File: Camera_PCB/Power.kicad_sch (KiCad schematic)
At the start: 50 parts, among them J3 USB_C_Receptacle_PowerOnly_6P, Q3 AO3400A, Q4 AO3400A, SW2 SW_Push, U4 BQ297xy

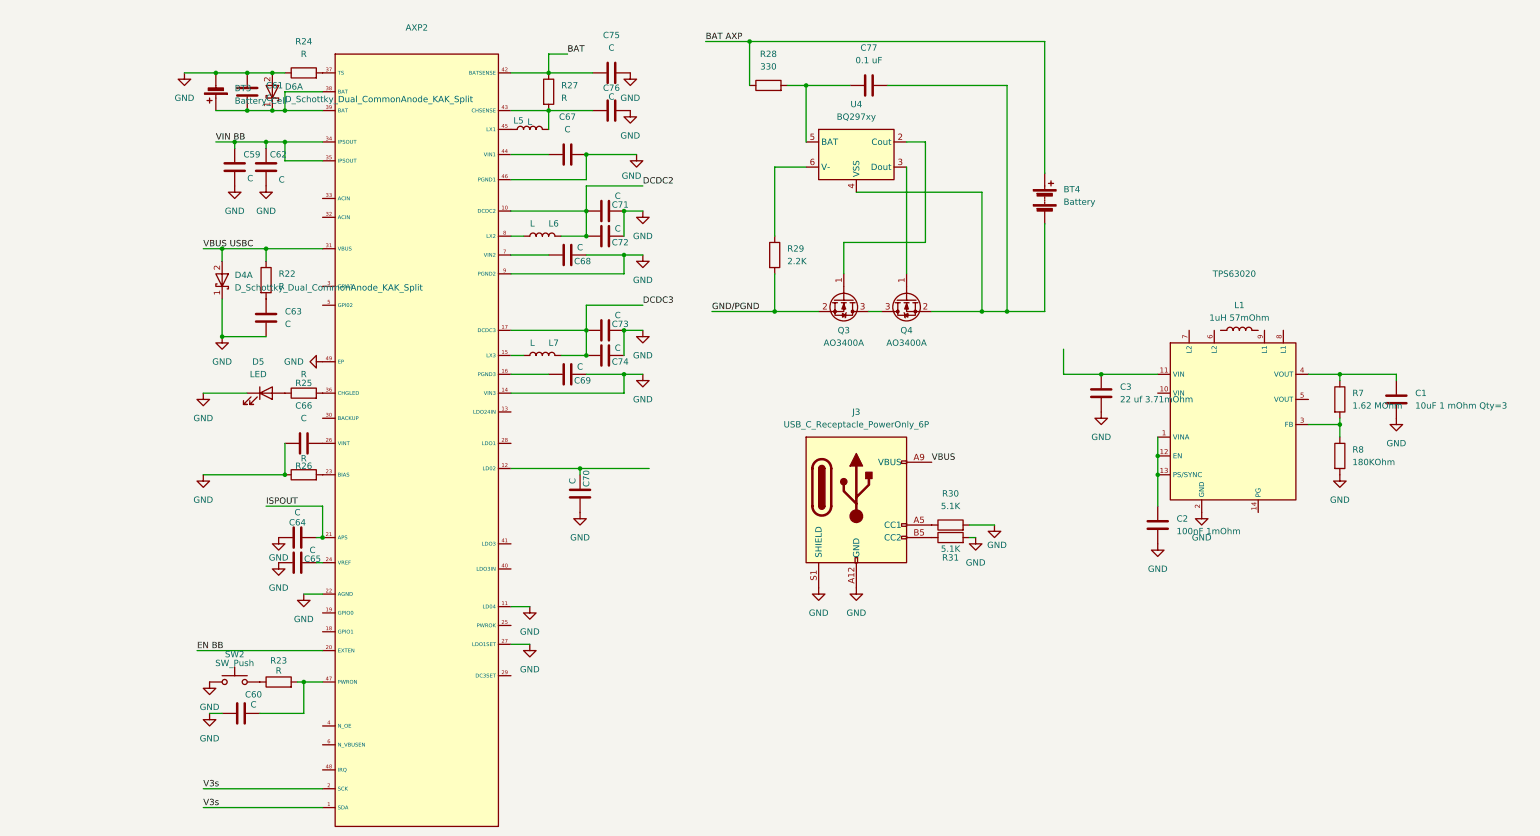
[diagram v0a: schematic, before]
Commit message: Updated Component Values for Power
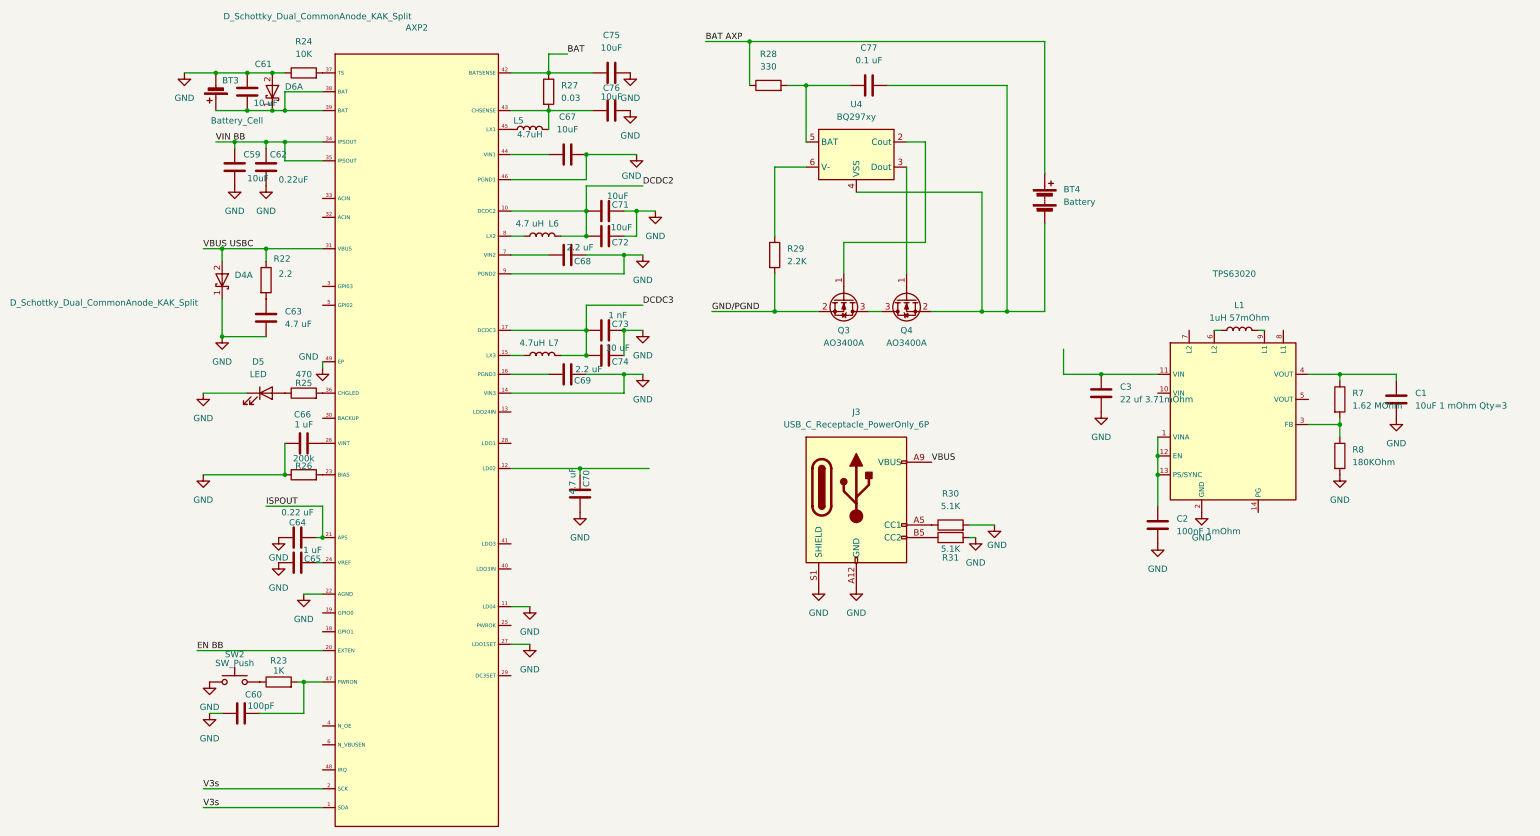
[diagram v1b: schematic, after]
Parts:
- C59, C67, C71, C72, C75, C76: value C -> 10uF
- C60: value C -> 100pF
- C61, C74: value C -> 10 uF
- C62: value C -> 0.22uF
- C63, C70: value C -> 4.7 uF
- C64: value C -> 0.22 uF
- C65, C66: value C -> 1 uF
- C68, C69: value C -> 2.2 uF
- C73: value C -> 1 nF
- L5, L7: value L -> 4.7uH
- L6: value L -> 4.7 uH
- R22: value R -> 2.2
- R23: value R -> 1K
- R24: value R -> 10K
- R25: value R -> 470
- R26: value R -> 200k
- R27: value R -> 0.03
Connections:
- net at TPS63020.6 (L2): now also L1.1
- net at TPS63020.9 (L1): now also L1.2
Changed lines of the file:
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@@
 	)
 	(junction
-		(at 114.3 60.96)
-		(diameter 0)
-		(color 0 0 0 0)
-	)
-	(junction
 		(at 43.18 40.64)
 		(diameter 0)
@@
 	)
 	(junction
+		(at 116.84 60.96)
+		(diameter 0)
+		(color 0 0 0 0)
+	)
+	(junction
 		(at 106.68 90.17)
 		(diameter 0)
@@
 	(wire
 		(pts
+			(xy 233.68 85.09) (xy 234.95 85.09)
+		)
+		(stroke
+			(width 0)
+			(type default)
+		)
+	)
+	(wire
+		(pts
 			(xy 222.25 114.3) (xy 222.25 120.65)
 		)
@@
 	(wire
 		(pts
+			(xy 53.34 92.71) (xy 53.34 91.44)
+		)
+		(stroke
+			(width 0)
+			(type default)
+		)
+	)
+	(wire
+		(pts
 			(xy 29.21 97.79) (xy 38.1 97.79)
 		)
@@
 	(wire
 		(pts
+			(xy 116.84 60.96) (xy 120.65 60.96)
+		)
+		(stroke
+			(width 0)
+			(type default)
+		)
+	)
+	(wire
+		(pts
 			(xy 199.39 26.67) (xy 139.7 26.67)
 		)
@@
 	(wire
 		(pts
-			(xy 114.3 60.96) (xy 114.3 66.04)
+			(xy 116.84 60.96) (xy 116.84 66.04)
 		)
 		(stroke
@@
 	(wire
 		(pts
+			(xy 242.57 85.09) (xy 243.84 85.09)
+		)
+		(stroke
+			(width 0)
+			(type default)
+		)
+	)
+	(wire
+		(pts
 			(xy 259.08 93.98) (xy 259.08 95.25)
 		)
@@
 	(wire
 		(pts
-			(xy 114.3 60.96) (xy 118.11 60.96)
+			(xy 114.3 60.96) (xy 116.84 60.96)
 		)
 		(stroke
@@
 	(wire
 		(pts
+			(xy 116.84 66.04) (xy 114.3 66.04)
+		)
+		(stroke
+			(width 0)
+			(type default)
+		)
+	)
+	(wire
+		(pts
 			(xy 99.06 40.64) (xy 99.06 44.45)
 		)
@@
 			)
 		)
-		(property "Value" "C"
+		(property "Value" "2.2 uF"
 			(at 105.41 68.326 90)
 			(effects
@@
 			)
 		)
-		(property "Value" "C"
-			(at 39.37 160.782 90)
+		(property "Value" "100pF"
+			(at 40.894 161.036 90)
 			(effects
 				(font
@@
 			)
 		)
-		(property "Value" "R"
+		(property "Value" "470"
 			(at 49.53 93.98 90)
 			(effects
@@
 			)
 		)
-		(property "Value" "C"
+		(property "Value" "10uF"
 			(at 111.76 37.846 90)
 			(effects
@@
 			)
 		)
-		(property "Value" "C"
+		(property "Value" "0.22uF"
 			(at 44.45 54.61 0)
 			(effects
@@
 		(on_board yes)
 		(dnp no)
-		(fields_autoplaced yes)
 		(property "Reference" "BT3"
-			(at 35.56 36.1314 0)
+			(at 33.02 34.544 0)
 			(effects
 				(font
@@
 		)
 		(property "Value" "Battery_Cell"
-			(at 35.56 38.6714 0)
+			(at 30.734 42.672 0)
 			(effects
 				(font
@@
 			)
 		)
-		(property "Value" "C"
+		(property "Value" "4.7 uF"
 			(at 103.886 115.57 90)
 			(effects
@@
 			)
 		)
-		(property "Value" "C"
-			(at 105.41 92.456 90)
+		(property "Value" "2.2 uF"
+			(at 107.188 92.964 90)
 			(effects
 				(font
@@
 			)
 		)
-		(property "Value" "C"
+		(property "Value" "4.7 uF"
 			(at 45.72 83.8199 0)
 			(effects
@@
 			)
 		)
-		(property "Value" "C"
+		(property "Value" "1 uF"
 			(at 51.308 129.54 90)
 			(effects
@@
 			)
 		)
-		(property "Value" "R"
+		(property "Value" "200k"
 			(at 49.53 110.998 90)
 			(effects
@@
 	(symbol
 		(lib_id "power:GND")
-		(at 53.34 91.44 270)
+		(at 53.34 92.71 0)
 		(unit 1)
 		(exclude_from_sim no)
@@
 		(on_board yes)
 		(dnp no)
-		(fields_autoplaced yes)
 		(property "Reference" "#PWR038"
-			(at 46.99 91.44 0)
+			(at 53.34 99.06 0)
 			(effects
 				(font
@@
 		)
 		(property "Value" "GND"
-			(at 49.53 91.4399 90)
+			(at 48.514 90.424 0)
 			(effects
 				(font
 					(size 1.27 1.27)
 				)
-				(justify right)
+				(justify left)
 			)
 		)
 		(property "Footprint" ""
-			(at 53.34 91.44 0)
+			(at 53.34 92.71 0)
 			(effects
 				(font
@@
 		)
 		(property "Datasheet" ""
-			(at 53.34 91.44 0)
+			(at 53.34 92.71 0)
 			(effects
 				(font
@@
 		)
 		(property "Description" "Power symbol creates a global label with name \"GND\" , ground"
-			(at 53.34 91.44 0)
+			(at 53.34 92.71 0)
 			(effects
 				(font
@@
 			)
 		)
-		(property "Value" "L"
-			(at 95.25 42.926 90)
+		(property "Value" "4.7uH"
+			(at 95.25 45.466 90)
 			(effects
 				(font
@@
 			)
 		)
-		(property "Value" "C"
+		(property "Value" "10 uF"
 			(at 113.03 88.646 90)
 			(effects
@@
 			)
 		)
-		(property "Value" "C"
+		(property "Value" "10uF"
 			(at 113.03 57.912 90)
 			(effects
@@
 			)
 		)
-		(property "Value" "R"
+		(property "Value" "0.03"
 			(at 101.6 38.0999 0)
 			(effects
@@
 	(symbol
 		(lib_id "power:GND")
-		(at 118.11 60.96 0)
+		(at 120.65 60.96 0)
 		(unit 1)
 		(exclude_from_sim no)
@@
 		(fields_autoplaced yes)
 		(property "Reference" "#PWR046"
-			(at 118.11 67.31 0)
+			(at 120.65 67.31 0)
 			(effects
 				(font
@@
 		)
 		(property "Value" "GND"
-			(at 118.11 66.04 0)
+			(at 120.65 66.04 0)
 			(effects
 				(font
@@
 		)
 		(property "Footprint" ""
-			(at 118.11 60.96 0)
+			(at 120.65 60.96 0)
 			(effects
 				(font
@@
 		)
 		(property "Datasheet" ""
-			(at 118.11 60.96 0)
+			(at 120.65 60.96 0)
 			(effects
 				(font
@@
 		)
 		(property "Description" "Power symbol creates a global label with name \"GND\" , ground"
-			(at 118.11 60.96 0)
+			(at 120.65 60.96 0)
 			(effects
 				(font
@@
 			)
 		)
-		(property "Value" "C"
+		(property "Value" "0.22 uF"
 			(at 48.26 121.92 90)
 			(effects
@@
 			)
 		)
-		(property "Value" "R"
+		(property "Value" "1K"
 			(at 44.45 153.924 90)
 			(effects
@@
 			)
 		)
-		(property "Value" "R"
+		(property "Value" "10K"
 			(at 49.53 29.21 90)
 			(effects
@@
 			)
 		)
-		(property "Value" "C"
+		(property "Value" "1 nF"
 			(at 113.03 82.042 90)
 			(effects
@@
 			)
 		)
-		(property "Value" "C"
+		(property "Value" "10uF"
 			(at 111.76 27.94 90)
 			(effects
@@
 			)
 		)
-		(property "Value" "C"
+		(property "Value" "10uF"
 			(at 38.1 54.356 0)
 			(effects
@@
 		(on_board yes)
 		(dnp no)
-		(fields_autoplaced yes)
 		(property "Reference" "R22"
-			(at 44.45 73.6599 0)
+			(at 43.434 70.612 0)
 			(effects
 				(font
@@
 			)
 		)
-		(property "Value" "R"
-			(at 44.45 76.1999 0)
+		(property "Value" "2.2"
+			(at 44.45 73.66 0)
 			(effects
 				(font
@@
 			)
 		)
-		(property "Value" "C"
-			(at 113.03 64.516 90)
+		(property "Value" "10uF"
+			(at 113.792 64.262 90)
 			(effects
 				(font
@@
 		(on_board yes)
 		(dnp no)
-		(fields_autoplaced yes)
 		(property "Reference" "C66"
-			(at 49.53 100.33 90)
+			(at 49.276 102.108 90)
 			(effects
 				(font
@@
 			)
 		)
-		(property "Value" "C"
-			(at 49.53 102.87 90)
+		(property "Value" "1 uF"
+			(at 49.53 104.14 90)
 			(effects
 				(font
@@
 		)
 		(property "Value" "D_Schottky_Dual_CommonAnode_KAK_Split"
-			(at 35.56 76.4539 90)
+			(at -9.906 79.502 90)
 			(effects
 				(font
@@
 			)
 		)
-		(property "Value" "L"
+		(property "Value" "4.7uH"
 			(at 95.758 87.63 90)
 			(effects
@@
 			)
 		)
-		(property "Value" "C"
+		(property "Value" "10uF"
 			(at 102.87 44.45 90)
 			(effects
@@
 		)
 		(property "Value" "D_Schottky_Dual_CommonAnode_KAK_Split"
-			(at 45.72 38.3539 90)
+			(at 33.274 21.59 90)
 			(effects
 				(font
@@
 		(on_board yes)
 		(dnp no)
-		(fields_autoplaced yes)
 		(property "Reference" "C61"
-			(at 41.91 35.5599 0)
+			(at 39.624 31.242 0)
 			(effects
 				(font
@@
 			)
 		)
-		(property "Value" "C"
-			(at 41.91 38.0999 0)
+		(property "Value" "10 uF"
+			(at 39.37 39.116 0)
 			(effects
 				(font
@@
 			)
 		)
-		(property "Value" "L"
-			(at 95.758 63.5 90)
+		(property "Value" "4.7 uH"
+			(at 95.25 63.5 90)
 			(effects
 				(font

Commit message: 10/29 Footprint Additions
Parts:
- AXP2: Distributor (none) -> Aliexpress
- C1: value 10uF 1 mOhm Qty=3 -> 10u; footprint (none) -> Capacitor_SMD:C_0805_2012Metric_Pad1.18x1.45mm_HandSolder
- C2: value 100nF 1mOhm -> 100n; footprint (none) -> Capacitor_SMD:C_0603_1608Metric_Pad1.08x0.95mm_HandSolder
- C3: value 22 uf 3.71mOhm -> 22u; footprint (none) -> Capacitor_SMD:C_0805_2012Metric_Pad1.18x1.45mm_HandSolder
- C59, C67, C71, C72, C75, C76: value 10uF -> 10u; footprint (none) -> Capacitor_SMD:C_0805_2012Metric_Pad1.18x1.45mm_HandSolder
- C60: value 100pF -> 100p; footprint (none) -> Capacitor_SMD:C_0603_1608Metric_Pad1.08x0.95mm_HandSolder
- C61, C74: value 10 uF -> 10u; footprint (none) -> Capacitor_SMD:C_0805_2012Metric_Pad1.18x1.45mm_HandSolder
- C62: value 0.22uF -> 0.22u; footprint (none) -> Capacitor_SMD:C_0603_1608Metric_Pad1.08x0.95mm_HandSolder
- C63, C70: value 4.7 uF -> 4.7u; footprint (none) -> Capacitor_SMD:C_0805_2012Metric_Pad1.18x1.45mm_HandSolder
- C64: value 0.22 uF -> 0.22u; footprint (none) -> Capacitor_SMD:C_0603_1608Metric_Pad1.08x0.95mm_HandSolder
- C65, C66: value 1 uF -> 1u; footprint (none) -> Capacitor_SMD:C_0805_2012Metric_Pad1.18x1.45mm_HandSolder
- C68, C69: value 2.2 uF -> 2.2u; footprint (none) -> Capacitor_SMD:C_0805_2012Metric_Pad1.18x1.45mm_HandSolder
- C73: value 1 nF -> 1n; footprint (none) -> Capacitor_SMD:C_0603_1608Metric_Pad1.08x0.95mm_HandSolder
- C77: value 0.1 uF -> 0.1u; footprint (none) -> Capacitor_SMD:C_0603_1608Metric_Pad1.08x0.95mm_HandSolder
- J3: footprint (none) -> Connector_USB:USB_C_Receptacle_GCT_USB4085; DPN (none) -> USB4085-GF-A; Distributor (none) -> DigiKey
- TPS63020: DPN (none) -> TPS63020DSJT; Distributor (none) -> Digikey
- U4: DPN (none) -> BQ29700DSET; Distributor (none) -> Digikey

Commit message: Camera PCB Schematic review 1
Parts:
- removed BT3: Battery_Cell, symbol Device:Battery_Cell
- removed BT4: Battery, symbol Device:Battery
- removed C1, C59, C61, C67, C71, C72, C74, C75, C76: 10u, Capacitor_SMD:C_0805_2012Metric_Pad1.18x1.45mm_HandSolder, symbol Device:C
- removed C2: 100n, Capacitor_SMD:C_0603_1608Metric_Pad1.08x0.95mm_HandSolder, symbol Device:C
- removed C3: 22u, Capacitor_SMD:C_0805_2012Metric_Pad1.18x1.45mm_HandSolder, symbol Device:C
- removed C60: 100p, Capacitor_SMD:C_0603_1608Metric_Pad1.08x0.95mm_HandSolder, symbol Device:C
- removed C62, C64: 0.22u, Capacitor_SMD:C_0603_1608Metric_Pad1.08x0.95mm_HandSolder, symbol Device:C
- removed C63, C70: 4.7u, Capacitor_SMD:C_0805_2012Metric_Pad1.18x1.45mm_HandSolder, symbol Device:C
- removed C65, C66: 1u, Capacitor_SMD:C_0805_2012Metric_Pad1.18x1.45mm_HandSolder, symbol Device:C
- removed C68, C69: 2.2u, Capacitor_SMD:C_0805_2012Metric_Pad1.18x1.45mm_HandSolder, symbol Device:C
- removed C73: 1n, Capacitor_SMD:C_0603_1608Metric_Pad1.08x0.95mm_HandSolder, symbol Device:C
- removed C77: 0.1u, Capacitor_SMD:C_0603_1608Metric_Pad1.08x0.95mm_HandSolder, symbol Device:C
- removed D4, D6: D_Schottky_Dual_CommonAnode_KAK_Split, symbol Device:D_Schottky_Dual_CommonAnode_KAK_Split
- removed D5: LED, symbol Device:LED
- removed L1: 1uH 57mOhm, symbol Device:L
- removed L6: 4.7 uH, symbol Device:L
- removed L7: 4.7uH, symbol Device:L
- removed Q3, Q4: AO3400A, Package_TO_SOT_SMD:SOT-23, symbol Transistor_FET:AO3400A
- removed R22: 2.2, symbol Device:R
- removed R23: 1K, symbol Device:R
- removed R24: 10K, symbol Device:R
- removed R25: 470, symbol Device:R
- removed R26: 200k, symbol Device:R
- removed R27: 0.03, symbol Device:R
- removed R28: 330, symbol Device:R
- removed R29: 2.2K, symbol Device:R
- removed R30, R31: 5.1K, symbol Device:R
- removed R7: 1.62 MOhm, symbol Device:R
- removed R8: 180KOhm, symbol Device:R
- removed SW2: SW_Push, symbol Switch:SW_Push
- removed TPS63020: ~, BackupCamCustomParts:IC_TPS63020DSJT, symbol Senior:TPS63020
- removed U4: BQ297xy, Package_SON:WSON-6_1.5x1.5mm_P0.5mm, symbol Battery_Management:BQ297xy
- added BT1: Battery_Cell, symbol Device:Battery_Cell
- added C35, C42, C43, C50, C54, C56, C58, C6, C62, C63: 10u, symbol Device:C_Small
- added C36, C44, C61, C73, C74: 4.7u, symbol Device:C_Small
- added C45, C55, C57, C59, C60: 0.1u, symbol Device:C_Small
- added C48, C49, C5: 1u, symbol Device:C_Small
- added L8, L9: 4.7uH, symbol Device:L
- added R14: 0.03, symbol Device:R_Small_US
- added R15: 200k, symbol Device:R_Small_US
- added R16, R17: 5.1k, symbol Device:R_Small_US
- added R20, R21: 1k, symbol Device:R_Small_US
- added R22, R23: 0, symbol Device:R_Small_US
- added SW1: PWR, symbol Switch:SW_MEC_5E
- added SW2: RST, symbol Switch:SW_MEC_5E
- U1: renamed from AXP2; value ~ -> AXP203; symbol Senior:AXP203 -> custom_chips:AXP203; Distributor Aliexpress -> (none)
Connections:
- net BAT is gone; now on net VBAT: U1.42 (BATSENSE)
- net ISPOUT is gone; now on net VIPS: U1.21 (APS)
- net VIN BB is gone; now on net VIPS: U1.34 (IPSOUT), U1.35 (IPSOUT)
- net GND: now also U1.16 (PGND3), U1.29 (DC3SET), BT1.2 (-), C35.2, C36.2, C42.1, C43.1, C50.1, C54.1, C55.1, C56.1, C57.1, C58.1, C6.2, C61.1, C62.1, C63.1, C73.1, C74.1, R16.2, R17.2; no longer U1.11 (LD04), U1.14 (VIN3), U1.22 (AGND), U1.27 (LDO1SET)
- net VBUS: now also U1.32 (ACIN), U1.33 (ACIN), C50.2
- net at J3.A5 (CC1): now also R17.1
- net at J3.B5 (CC2): now also R16.1
- net VIPS: now reaches U1.7 (VIN2)
- net VIPS: now also U1.14 (VIN3), U1.44 (VIN1), C36.1, C42.2, C43.2, C44.1, C45.1, C58.2, R22.1
- net at U1.47 (PWRON): now also C59.1, R20.2
- net CHGLED: now reaches U1.36 (CHGLED)
- net at L5.2, U1.43 (CHSENSE): now also C5.2, C6.1, R14.1
- net VBAT: now reaches U1.38 (BAT), U1.39 (BAT)
- net VBAT: now also BT1.1 (+), C35.1, C5.1, R14.2
- net +3V0: now reaches U1.12 (LD02)
- net +3V0: now also C63.2
- net at U1.24 (VREF): now also C48.1
- net at U1.23 (BIAS): now also R15.2
- net +3V3: now reaches U1.13 (LDO24IN)
- net +3V3: now also C62.2
- net at U1.15 (LX3): now also L9.1
- net PGOOD: now reaches U1.25 (PWROK)
- net VINT: now reaches U1.26 (VINT)
- net VINT: now also U1.27 (LDO1SET), C49.2
- net VCC-RTC: now reaches U1.28 (LDO1)
- net VCC-RTC: now also C61.2
- net at U1.4 (N_OE): now also C60.1, R21.2
- net at U1.41 (LDO3): now also C74.2
- net IRQ: now reaches U1.48 (IRQ/WAKEUP)
- net at U1.6 (N_VBUSEN): now also R22.2, R23.2
- net at U1.8 (LX2): now also L8.1
- net DCDC2 renamed +1V2
- net +1V2: now also C54.2, C55.2, L8.2
- net DCDC3 renamed +1V8
- net +1V8: now also C56.2, C57.2, L9.2
- net EN BB renamed PWREN
- net V3s renamed TWI0_SCK
- net TWI0_SCK: no longer U1.1 (SDA)
- net VBUS USBC: no longer names the net of U1.31 (VBUS)
- new net: R21.1, SW2.3 (K)
- new net: C73.2, U1.11 (LD04)
- new net: R20.1, SW1.3 (K)
- new net GNDA: C44.2, C45.2, C48.2, C49.1, C59.2, C60.2, R15.1, R23.1, SW1.2, SW2.2, U1.22 (AGND)
- new net TWI0_SDA: U1.1 (SDA)
- no-connect marks 0 -> 7
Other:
- note added: "* Place decoupling caps as close to sense pins as possinle. Use 0603"
- note added: "3.7V Lithium Ion Battery W/ built in UV/OC protection Target 8Ah"
- note added: "According to the allwinner reference design and https://github.com/FunKey- Project/FunKey-S-Hardware/issues/2 Default voltages for AXP203/V3S reference design are DC2=1.25V, DC3=1.8V (when tied to GND), LDO1=3.3V (when tied to VINT), LDO2=3.0V"
- note added: "Connect VBUS to ACIN instead of VBUS pin because VBUS pin is Limited to 500mA"
- note added: "Keep VCC-RTC separate for low noise"
- note added: "PWR button intended to be exposed Reset button intended to be internal"
- note added: "Use +/-1% 0603 resistor for 200k R (for fuel gauge)"
- note added: "VCC-RTC is 3.3V"
- moved on the sheet: J3, L5, U1
